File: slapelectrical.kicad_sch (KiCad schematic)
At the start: 7 parts, among them U1 Teensy4.1, U2 LM2596S-5

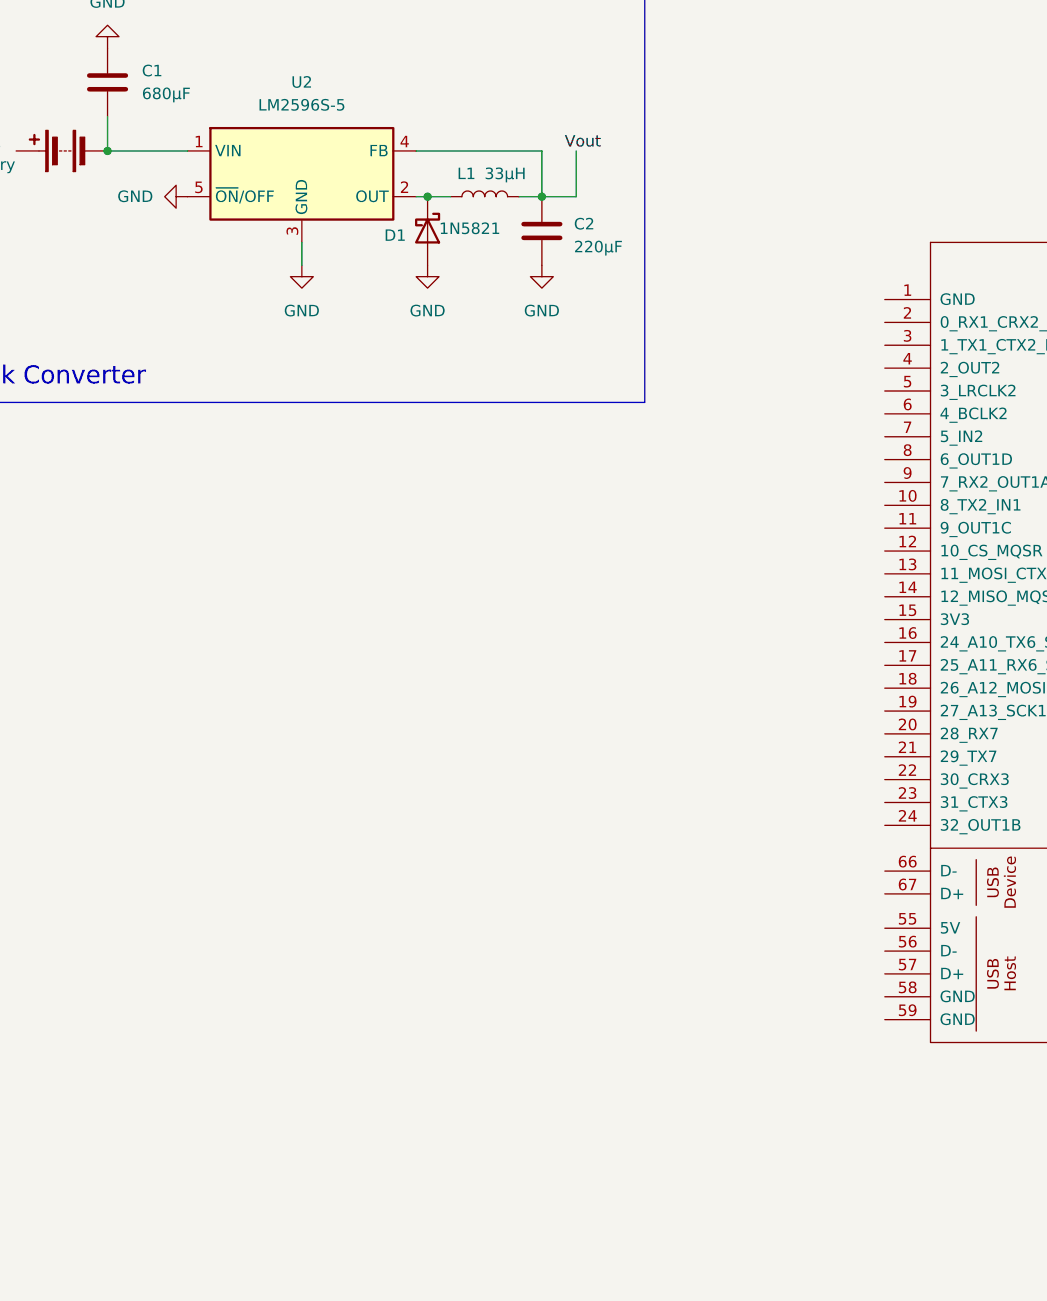
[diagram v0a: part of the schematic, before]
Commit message: added three vesc for testbench
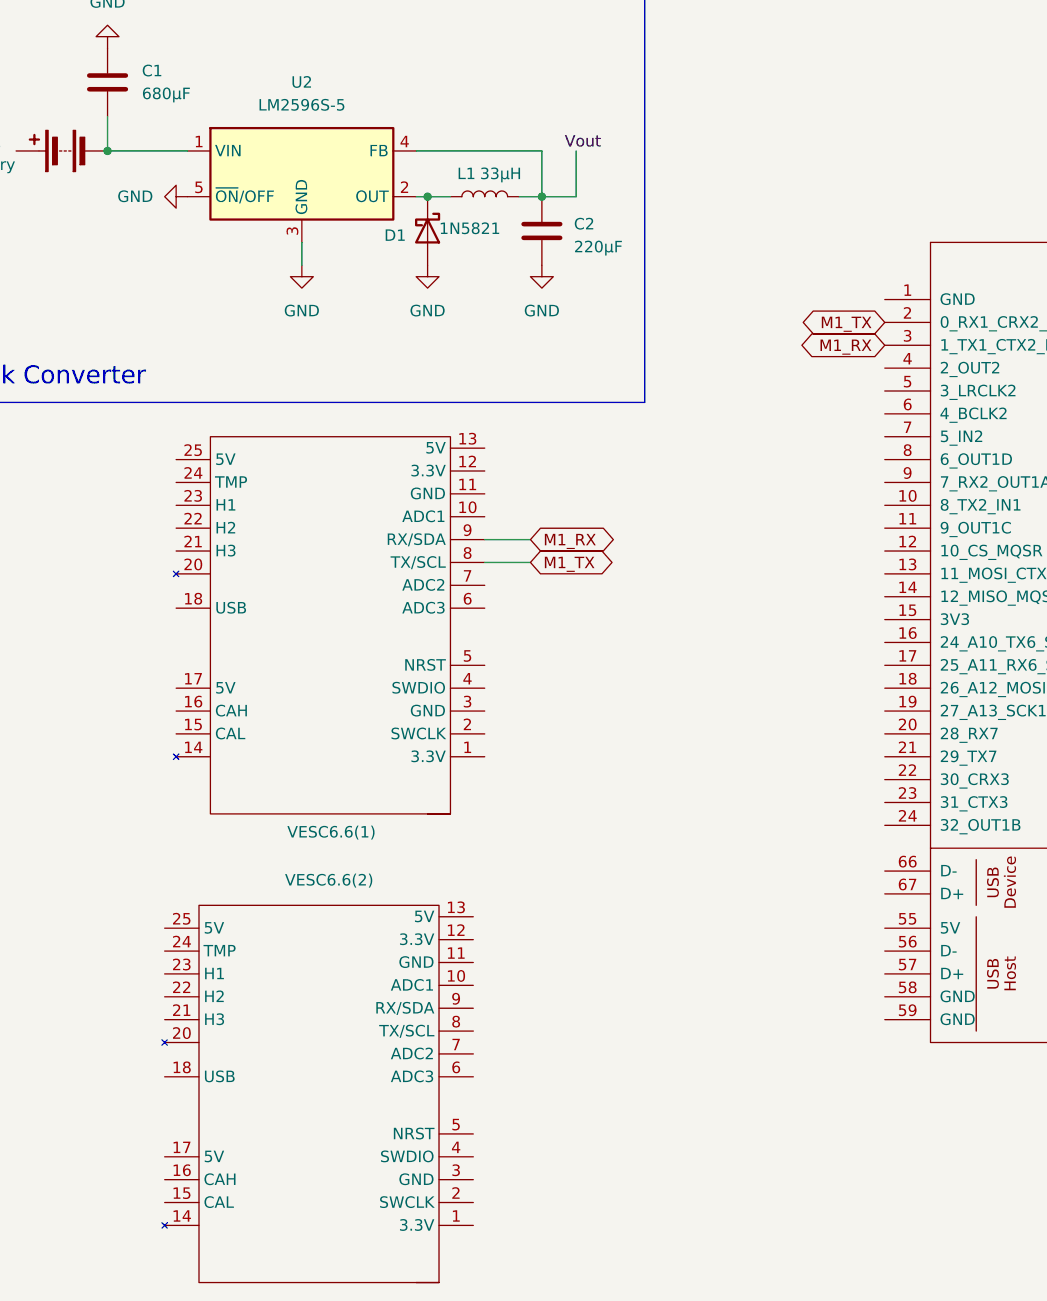
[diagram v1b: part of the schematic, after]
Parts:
- added VESC6.6(1), VESC6.6(2): ~, symbol Transistor_BJT:FSESC6.7
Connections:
- net M1_TX: now reaches U1.2 (0_RX1_CRX2_CS1)
- net M1_TX: now also VESC6.6(1).8 (TX/SCL)
- net M1_RX: now reaches U1.3 (1_TX1_CTX2_MISO1)
- net M1_RX: now also VESC6.6(1).9 (RX/SDA)

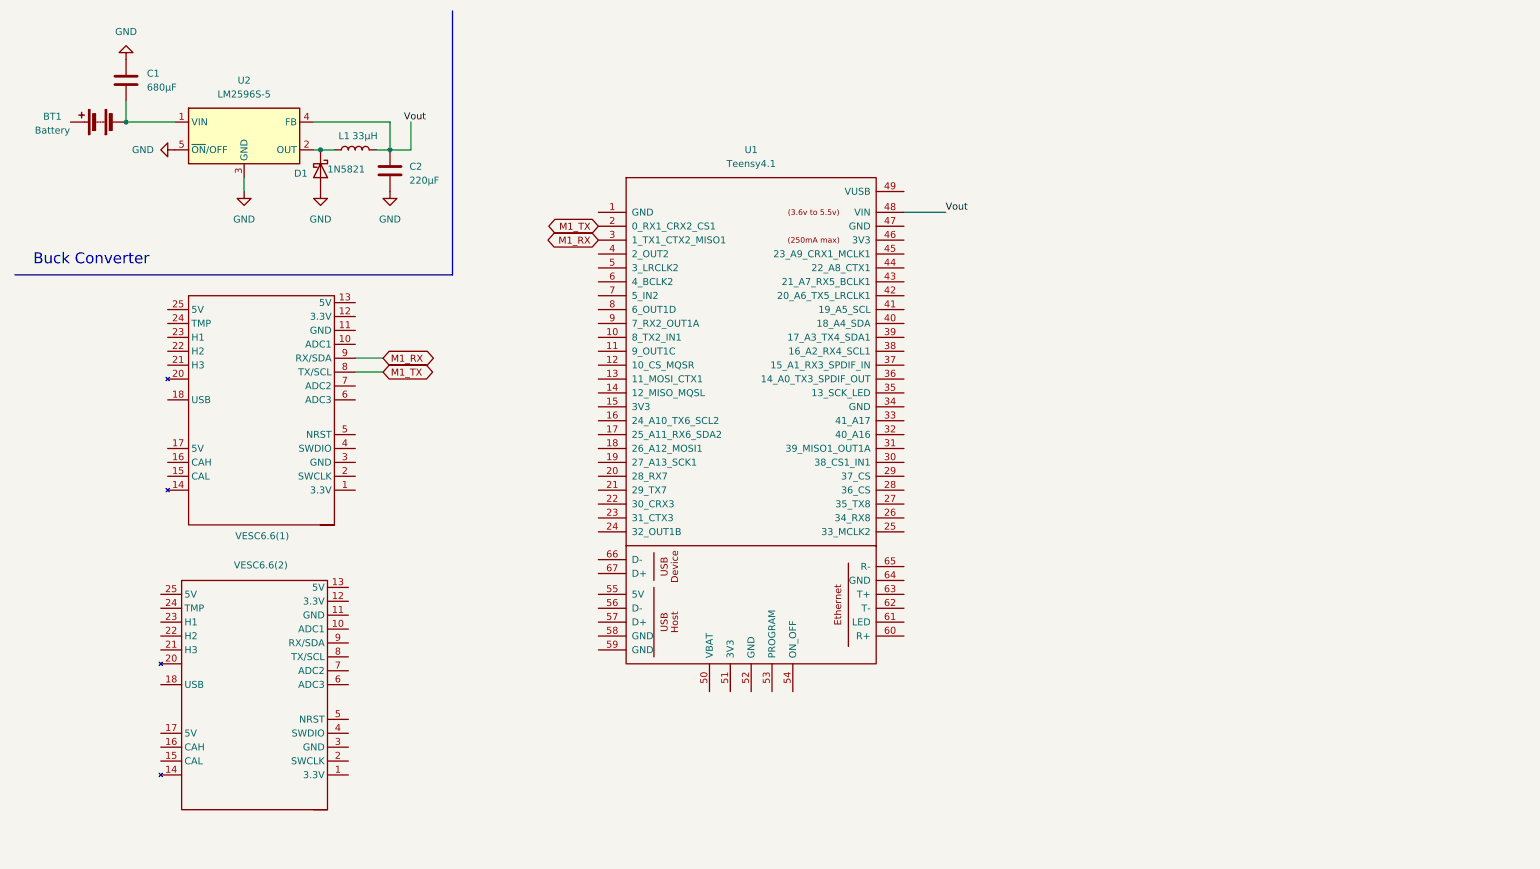
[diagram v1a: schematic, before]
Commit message: added three magnetic encoders
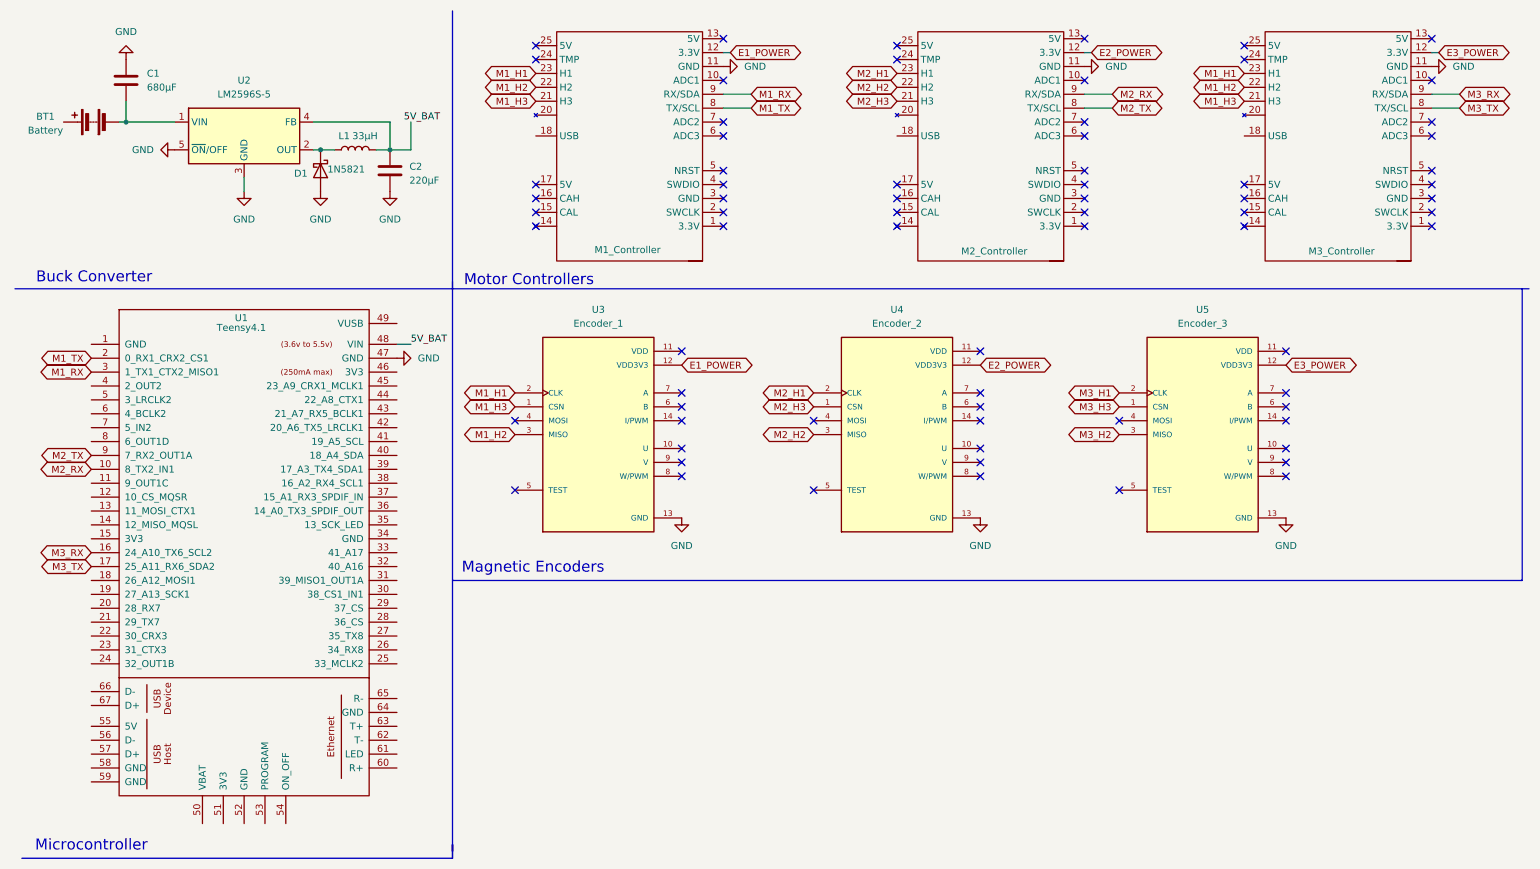
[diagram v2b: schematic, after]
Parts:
- removed VESC6.6(2): ~, symbol Transistor_BJT:FSESC6.7
- added M2_Controller, M3_Controller: ~, symbol Transistor_BJT:FSESC6.7
- added U3: Encoder_1, AS5047P-ATSM:SOP65P640X120-14N, symbol AS5047P-ATSM:AS5047P-ATSM
- added U4: Encoder_2, AS5047P-ATSM:SOP65P640X120-14N, symbol AS5047P-ATSM:AS5047P-ATSM
- added U5: Encoder_3, AS5047P-ATSM:SOP65P640X120-14N, symbol AS5047P-ATSM:AS5047P-ATSM
- renumbered VESC6.6(1) to M1_Controller
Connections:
- net GND: now also M1_Controller.11 (GND), U1.47 (GND), M2_Controller.11 (GND), M3_Controller.11 (GND), U3.13 (GND), U4.13 (GND), U5.13 (GND)
- net M2_RX: now reaches U1.10 (8_TX2_IN1)
- net M2_RX: now also M2_Controller.9 (RX/SDA)
- net M3_RX: now reaches U1.16 (24_A10_TX6_SCL2)
- net M3_RX: now also M3_Controller.9 (RX/SDA)
- net M3_TX: now reaches U1.17 (25_A11_RX6_SDA2)
- net M3_TX: now also M3_Controller.8 (TX/SCL)
- net M2_TX: now reaches U1.9 (7_RX2_OUT1A)
- net M2_TX: now also M2_Controller.8 (TX/SCL)
- net E1_POWER: now reaches M1_Controller.12 (3.3V)
- net E1_POWER: now also U3.12 (VDD3V3)
- net M1_H3: now reaches M1_Controller.21 (H3)
- net M1_H3: now also M3_Controller.21 (H3), U3.1 (CSN)
- net M1_H2: now reaches M1_Controller.22 (H2)
- net M1_H2: now also M3_Controller.22 (H2), U3.3 (MISO)
- net M1_H1: now reaches M1_Controller.23 (H1)
- net M1_H1: now also M3_Controller.23 (H1), U3.2 (CLK)
- net Vout renamed 5V_BAT
- new net E2_POWER: M2_Controller.12 (3.3V), U4.12 (VDD3V3)
- new net E3_POWER: M3_Controller.12 (3.3V), U5.12 (VDD3V3)
- new net M2_H1: M2_Controller.23 (H1), U4.2 (CLK)
- new net M2_H2: M2_Controller.22 (H2), U4.3 (MISO)
- new net M2_H3: M2_Controller.21 (H3), U4.1 (CSN)
- new net M3_H1: U5.2 (CLK)
- new net M3_H2: U5.3 (MISO)
- new net M3_H3: U5.1 (CSN)
- no-connect marks 0 -> 72
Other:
- note added: "Magnetic Encoders"
- note added: "Microcontroller"
- note added: "Motor Controllers"
- moved on the sheet: BT1, M1_Controller, U1

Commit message: Added and wired IMU
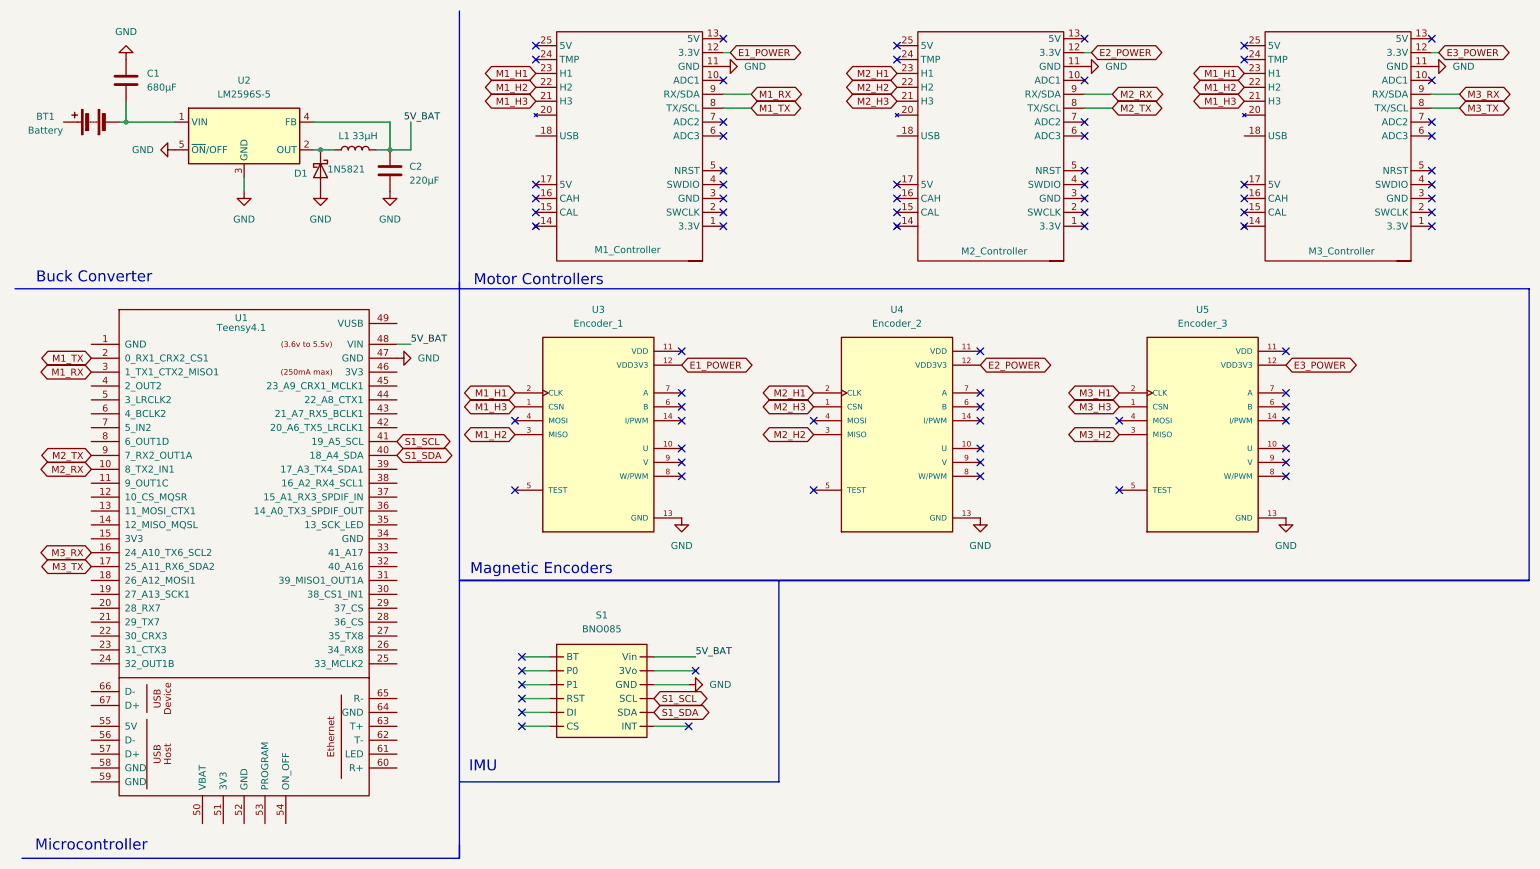
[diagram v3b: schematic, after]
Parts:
- added S1: BNO085, symbol BNO058:BNO058
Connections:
- net 5V_BAT: now also S1. (Vin)
- net GND: now also S1. (Vin)
- net S1_SDA: now reaches U1.40 (18_A4_SDA)
- net S1_SDA: now also S1. (Vin)
- net S1_SCL: now reaches U1.41 (19_A5_SCL)
- net S1_SCL: now also S1. (Vin)
- no-connect marks 72 -> 80
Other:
- note added: "IMU"
